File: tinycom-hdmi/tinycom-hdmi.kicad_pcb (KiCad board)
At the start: 2 copper layers, 45.2 x 45.2 mm, 82 parts, among them J1 MICRO_SD_HINGE, P1 CONN_02X10, P2 CONN_02X10, P4 USB_OTG, U1 SY8008BAAC, U10 admp411, U2 AXP209, U3 SY8008BAAC, U4 RTL8188, U5 rainsun-antenna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

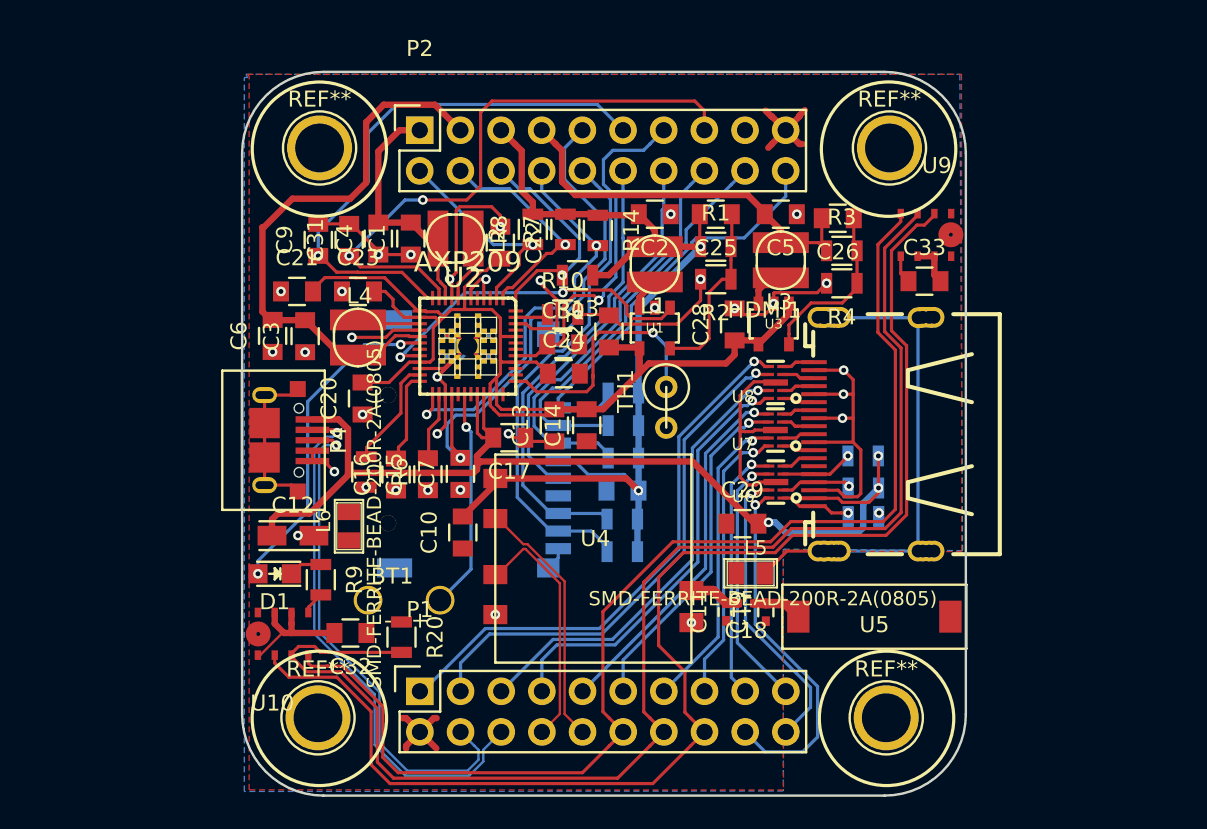
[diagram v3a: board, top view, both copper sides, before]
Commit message: update hdmi
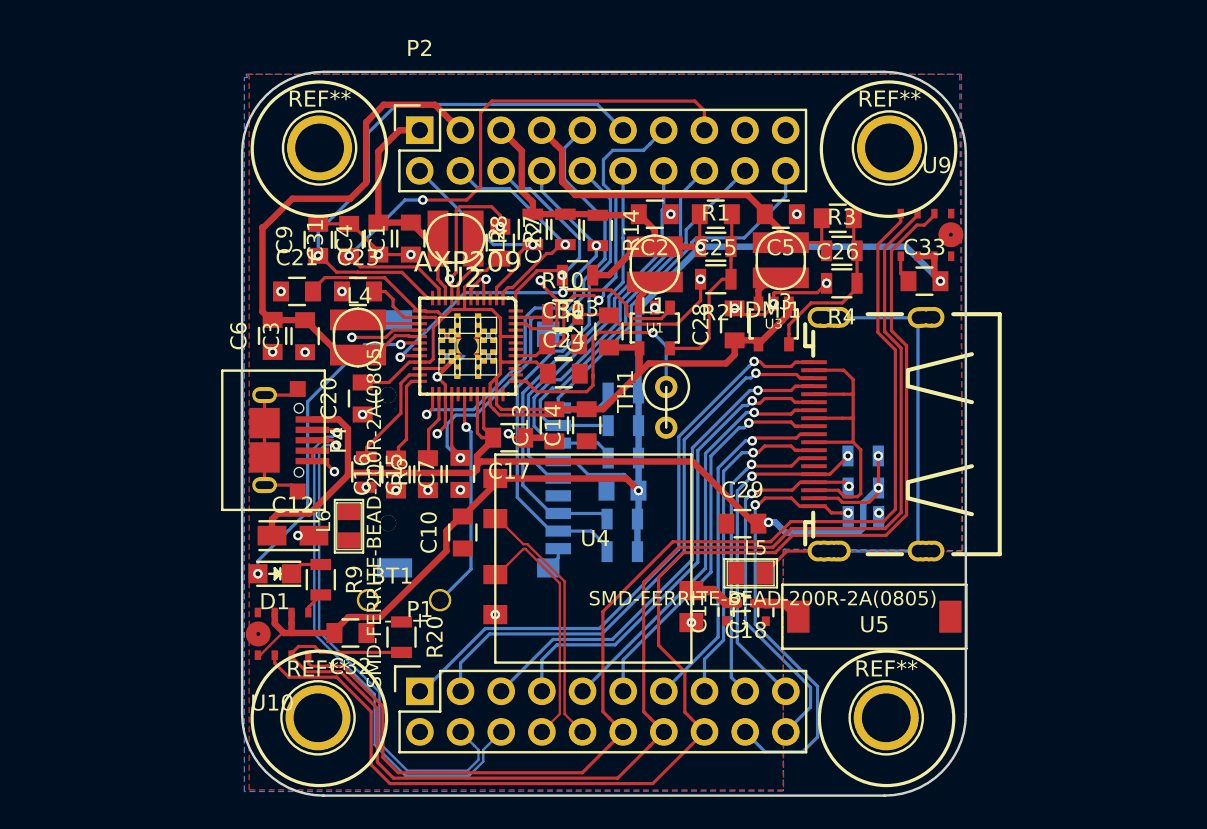
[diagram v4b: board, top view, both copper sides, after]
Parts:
- removed U6, U7, U8: RCLAMP0524P, tinycom:SLP2510P8
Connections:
- C14 pad 1: Net-(C14-Pad1) -> GND
- HDMI1 pad 1: Net-(HDMI1-Pad1) -> HTX2_P
- HDMI1 pad 10: Net-(HDMI1-Pad10) -> HTXC_P
- HDMI1 pad 12: Net-(HDMI1-Pad12) -> HTXC_N
- HDMI1 pad 13: Net-(HDMI1-Pad13) -> HCEC
- HDMI1 pad 15: Net-(HDMI1-Pad15) -> HCSL
- HDMI1 pad 16: Net-(HDMI1-Pad16) -> HSDA
- HDMI1 pad 19: Net-(HDMI1-Pad19) -> HHPD
- HDMI1 pad 3: Net-(HDMI1-Pad3) -> HTX2_N
- HDMI1 pad 4: Net-(HDMI1-Pad4) -> HTX1_P
- HDMI1 pad 6: Net-(HDMI1-Pad6) -> HTX1_N
- HDMI1 pad 7: Net-(HDMI1-Pad7) -> HTX0_P
- HDMI1 pad 9: Net-(HDMI1-Pad9) -> HTX0_N
- R11 pad 1: Net-(HDMI1-Pad15) -> HCSL
- R12 pad 2: Net-(HDMI1-Pad19) -> HHPD
- R5 pad 2: Net-(HDMI1-Pad16) -> HSDA
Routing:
- net VCC_33: track 74.6 -> 102.4 mm, vias 2 -> 3
- net GND: track 134.9 -> 111.7 mm, vias 35 -> 32
- net HCSL: track 16.2 -> 21.6 mm, vias 1 -> 2
- net HHPD: track 22.6 -> 27.9 mm, vias 1 -> 2
- net HSDA: track 18.5 -> 23.9 mm, vias 1 -> 2
- net Net-(HDMI1-Pad15): track 4.55 -> 0.00 mm, vias 1 -> 0
- net Net-(HDMI1-Pad19): track 4.46 -> 0.00 mm, vias 1 -> 0
- net Net-(HDMI1-Pad16): track 4.44 -> 0.00 mm, vias 1 -> 0
- net HCEC: track 16.2 -> 19.2 mm
- net HTX0_N: track 21.4 -> 24.4 mm
- net HTXC_N: track 17.7 -> 20.6 mm
- net HTX2_P: track 34.6 -> 37.5 mm
- net HTX1_P: track 28.6 -> 31.5 mm
- net HTX0_P: track 23.1 -> 26.0 mm
- net HTXC_P: track 19.3 -> 22.2 mm
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
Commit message: tinycom-hdmi rev2
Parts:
- moved L6 4.87 mm to (126.3, 107.9), turned to 180 degrees
- moved C12 3.85 mm to (131.5, 108.4), turned to 270 degrees
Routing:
- net GND: track 111.7 -> 126.7 mm, vias 32 -> 33
- net +5V: track 65.4 -> 61.5 mm
- net Net-(L6-Pad1): track 10.4 -> 13.6 mm
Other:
- board text added: "Tinycom-HDMI rev. 2"
- board text removed: "rev. 1"
